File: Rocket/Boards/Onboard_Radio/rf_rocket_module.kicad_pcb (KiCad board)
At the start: 4 copper layers, 55 x 65 mm, 98 parts, among them J1 CAN1_T, J19 Backup Power, J2 CAN2_T, J3 DB9 Microfit, J4 USB_B_Micro, J5 SWD JST PH, J6 DB9 Microfit, Q1 DMP6023LFG, SW1 On Switch, U1 SX1262IMLTRT, U2 TCAN1046, U3 STM32G0B1RCTx, U4 AZ1117C-5.0, U5 TPS2121RUXR, U6 PE4259 RF Switch, U7 AZ1117C-3.3, Y1 8MHz

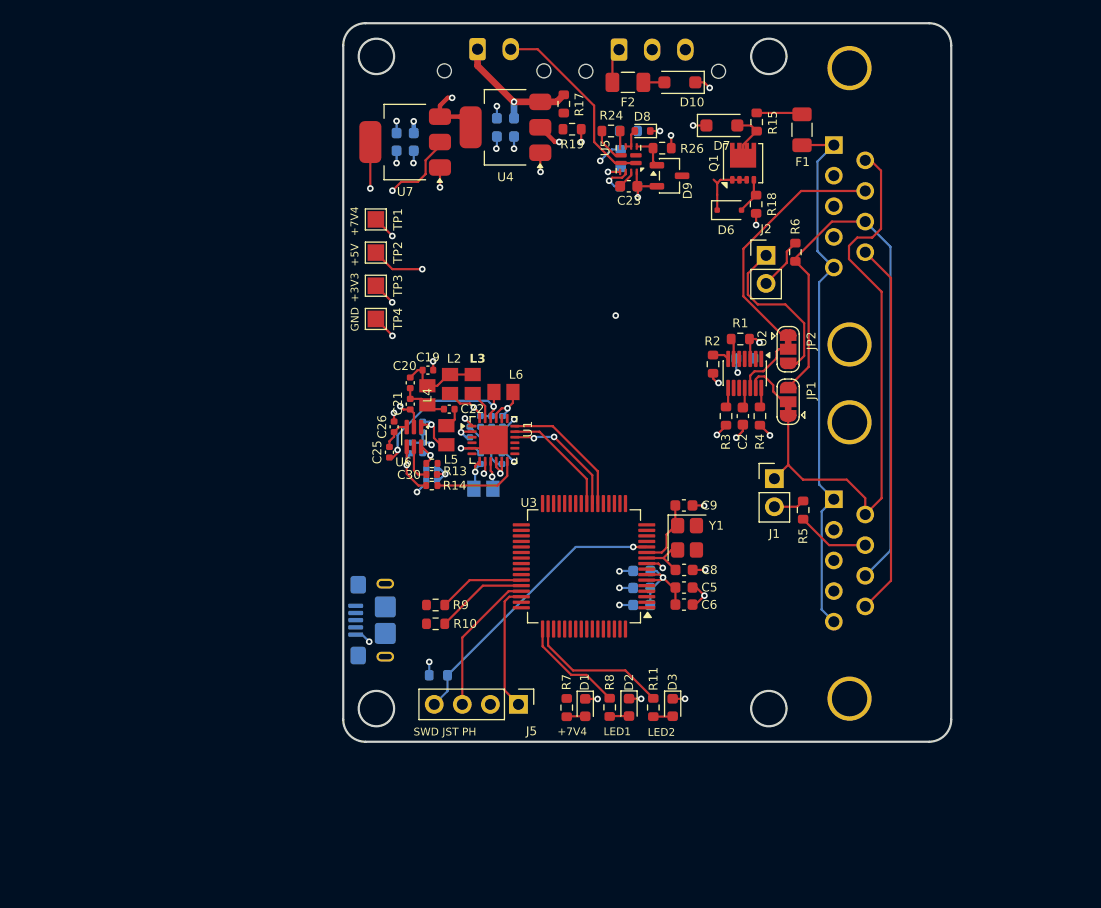
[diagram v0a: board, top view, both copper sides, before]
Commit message: schematic bom needs updating and traces need finishing
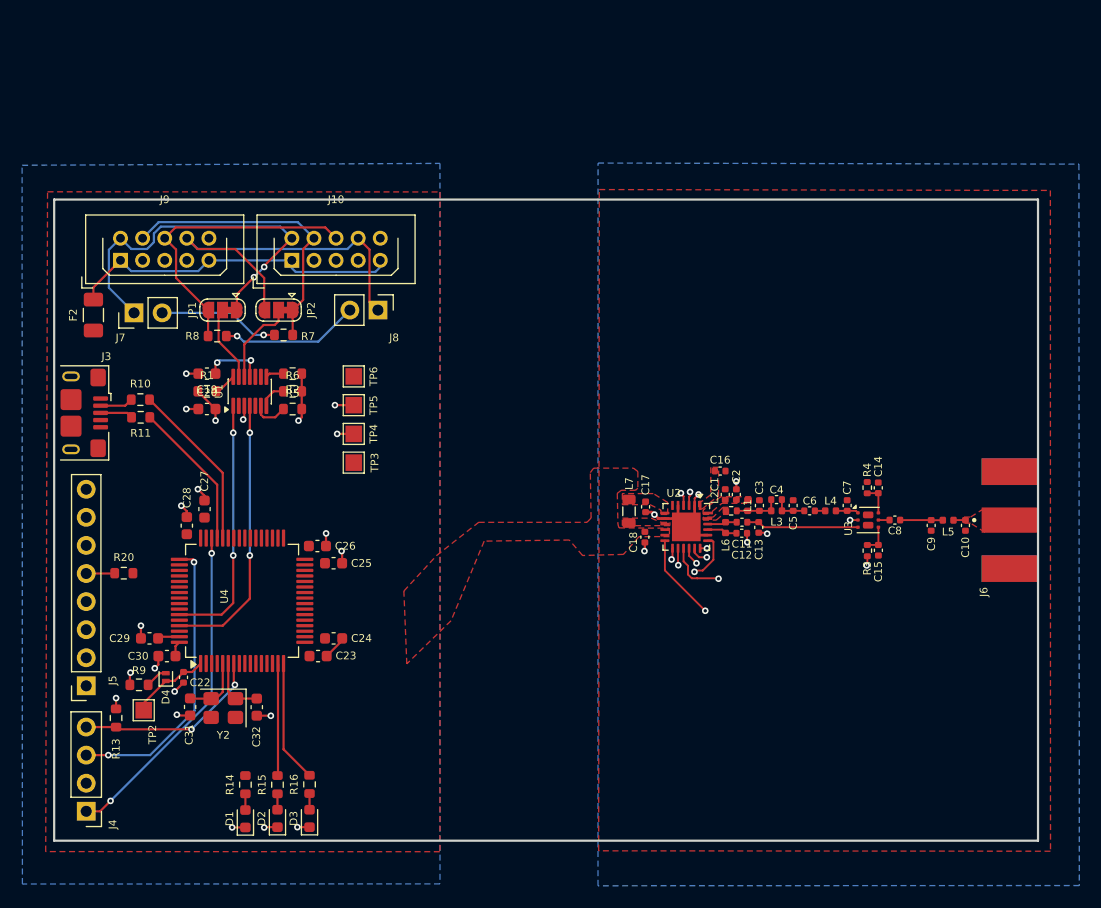
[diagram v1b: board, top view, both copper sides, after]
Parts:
- removed C21: C, Capacitor_SMD:C_0402_1005Metric
- removed D10, D7: 9V 15.4VC, Diode_SMD:D_SOD-123F
- removed D6: 18V, Diode_SMD:D_SOD-323F
- removed D8: D_0.5VF, Diode_SMD:D_SOD-523
- removed D9: 2.5V Ref Zener, Package_TO_SOT_SMD:SOT-23-3
- removed F1: 5A, Fuse:Fuse_1206_3216Metric
- removed H1, H2, H3, H4: MountingHole, MountingHole:MountingHole_3.2mm_M3
- removed J1: CAN1_T, Connector_PinHeader_2.54mm:PinHeader_1x02_P2.54mm_Vertical
- removed J19: Backup Power, Connector_Molex:Molex_Micro-Fit_3.0_43650-0315_1x03_P3.00mm_Vertical
- removed J2: CAN2_T, Connector_PinHeader_2.54mm:PinHeader_1x02_P2.54mm_Vertical
- removed Q1: DMP6023LFG, Package_SON:Diodes_PowerDI3333-8
- removed R12: R, Resistor_SMD:R_0603_1608Metric
- removed R17: 14K3, Resistor_SMD:R_0603_1608Metric
- removed R18: 100K, Resistor_SMD:R_0603_1608Metric
- removed R19: 9K53, Resistor_SMD:R_0603_1608Metric
- removed R22: 22K, Resistor_SMD:R_0603_1608Metric
- removed R23: 15K, Resistor_SMD:R_0603_1608Metric
- removed R24: 6K2, Resistor_SMD:R_0603_1608Metric
- removed R25: 4K7, Resistor_SMD:R_0603_1608Metric
- removed R26: 1K5, Resistor_SMD:R_0603_1608Metric
- removed SW1: On Switch, Connector_Molex:Molex_Micro-Fit_3.0_43650-0215_1x02_P3.00mm_Vertical
- removed TP1: 7V4, TestPoint:TestPoint_Pad_1.5x1.5mm
- removed U5: TPS2121RUXR, Package_DFN_QFN:Texas_VQFN-HR-12_2x2.5mm_P0.5mm
- removed U6: PE4259 RF Switch, Package_TO_SOT_SMD:SOT-363_SC-70-6
- removed U7: AZ1117C-3.3, Package_TO_SOT_SMD:SOT-223-3_TabPin2
- removed Y1: 8MHz, Crystal:Crystal_SMD_Abracon_ABM8G-4Pin_3.2x2.5mm
- added D4: D_Schottky, Diode_SMD:D_SOD-882, F.Cu at (115.6, 114.2)
- added J10: M80-5301042, Connector_Harwin:Harwin_LTek-Male_2x05_P2.00mm_Vertical, F.Cu at (127.0, 76.5)
- added J7: CAN1_T, Connector_PinHeader_2.54mm:PinHeader_1x02_P2.54mm_Vertical, F.Cu at (112.7, 81.2)
- added J8: CAN2_T, Connector_PinHeader_2.54mm:PinHeader_1x02_P2.54mm_Vertical, F.Cu at (134.8, 81.0)
- added J9: M80-5301042, Connector_Harwin:Harwin_LTek-Male_2x05_P2.00mm_Vertical, F.Cu at (111.5, 76.5)
- added L7: 15uH, Inductor_SMD:L_0805_2012Metric, F.Cu at (157.5, 99.2)
- added R16: 220R, Resistor_SMD:R_0603_1608Metric, F.Cu at (128.6, 123.9)
- added R20: 0R, Resistor_SMD:R_0603_1608Metric, F.Cu at (111.8, 104.8)
- added TP5: 3V3, TestPoint:TestPoint_Pad_1.5x1.5mm, F.Cu at (132.6, 89.6)
- added TP6: GND, TestPoint:TestPoint_Pad_1.5x1.5mm, F.Cu at (132.6, 87.0)
- added Y2: 12MHz, Crystal:Crystal_SMD_Abracon_ABM8G-4Pin_3.2x2.5mm, F.Cu at (120.8, 117.0)
- C1: value 100nF -> 47pF; footprint Capacitor_SMD:C_0603_1608Metric -> Capacitor_SMD:C_0402_1005Metric; moved to F.Cu
- C10: value C -> 3.3pF; moved to F.Cu
- C11: value 22uF -> 2.4pF; footprint Capacitor_SMD:C_0603_1608Metric -> Capacitor_SMD:C_0402_1005Metric; moved to F.Cu
- C12: value 10uF -> 1.8pF; footprint Capacitor_SMD:C_0603_1608Metric -> Capacitor_SMD:C_0402_1005Metric; moved to F.Cu
- C13: value 22uF -> ???; footprint Capacitor_SMD:C_0603_1608Metric -> Capacitor_SMD:C_0402_1005Metric; moved to F.Cu
- C14: value 10uF -> 1nF; footprint Capacitor_SMD:C_0603_1608Metric -> Capacitor_SMD:C_0402_1005Metric; moved to F.Cu
- C15: value 470nF -> 1nF; moved to F.Cu
- C16: value 100nF -> 1uF; moved to F.Cu
- C17: value C -> 470nF; moved to F.Cu
- C18: value C -> 100nF; moved to F.Cu
- C19, C20, C25: value C -> 100nF; footprint Capacitor_SMD:C_0402_1005Metric -> Capacitor_SMD:C_0603_1608Metric
- C2: value 100nF -> 47pF; footprint Capacitor_SMD:C_0603_1608Metric -> Capacitor_SMD:C_0402_1005Metric
- C22: value C -> 100n
- C24: value C -> 4.7uF; footprint Capacitor_SMD:C_0402_1005Metric -> Capacitor_SMD:C_0603_1608Metric; moved to F.Cu
- C26, C30: value C -> 4.7uF; footprint Capacitor_SMD:C_0402_1005Metric -> Capacitor_SMD:C_0603_1608Metric
- C27: value C -> 100nF; footprint Capacitor_SMD:C_0402_1005Metric -> Capacitor_SMD:C_0603_1608Metric; moved to F.Cu
- C28: value 1nF -> 4.7uF; footprint Capacitor_SMD:C_0402_1005Metric -> Capacitor_SMD:C_0603_1608Metric; moved to F.Cu
- C29: value 1nF -> 100nF; footprint Capacitor_SMD:C_0402_1005Metric -> Capacitor_SMD:C_0603_1608Metric; moved to F.Cu
- C3: value 100nF -> ???; footprint Capacitor_SMD:C_0603_1608Metric -> Capacitor_SMD:C_0402_1005Metric; moved to F.Cu
- C31, C32: value C -> 27pF; footprint Capacitor_SMD:C_0402_1005Metric -> Capacitor_SMD:C_0603_1608Metric; moved to F.Cu
- C4: value 100nF -> 3.0pF; footprint Capacitor_SMD:C_0603_1608Metric -> Capacitor_SMD:C_0402_1005Metric; moved to F.Cu
- C5: value 4.7uF -> 5.6pF; footprint Capacitor_SMD:C_0603_1608Metric -> Capacitor_SMD:C_0402_1005Metric
- C6: value 4.7uF -> 39pF; footprint Capacitor_SMD:C_0603_1608Metric -> Capacitor_SMD:C_0402_1005Metric
- C7: value 100nF -> 1.8pF; footprint Capacitor_SMD:C_0603_1608Metric -> Capacitor_SMD:C_0402_1005Metric; moved to F.Cu
- C8: value 27pF -> 39pF; footprint Capacitor_SMD:C_0603_1608Metric -> Capacitor_SMD:C_0402_1005Metric
- C9: value 27pF -> 3.3pF; footprint Capacitor_SMD:C_0603_1608Metric -> Capacitor_SMD:C_0402_1005Metric
- J3: value DB9 Microfit -> USB_B_Micro; footprint Connector_Dsub:DSUB-9_Pins_Horizontal_P2.77x2.84mm_EdgePinOffset7.70mm_Housed_MountingHolesOffset9.12mm -> Connector_USB:USB_Micro-B_Amphenol_10118193-0001LF_Horizontal; moved to F.Cu
- J4: value USB_B_Micro -> SWD JST PH; footprint Connector_USB:USB_Micro-B_Amphenol_10118193-0001LF_Horizontal -> Connector_PinHeader_2.54mm:PinHeader_1x04_P2.54mm_Vertical; moved to F.Cu
- J5: value SWD JST PH -> Conn_01x08; footprint Connector_PinHeader_2.54mm:PinHeader_1x04_P2.54mm_Vertical -> Connector_PinSocket_2.54mm:PinSocket_1x08_P2.54mm_Vertical
- J6: value DB9 Microfit -> RFIO SMA; footprint Connector_Dsub:DSUB-9_Pins_Horizontal_P2.77x2.84mm_EdgePinOffset7.70mm_Housed_MountingHolesOffset9.12mm -> Library:JOHNSON_142-0701-841; moved to F.Cu
- L1: value 15uH -> 47nH; footprint Library:INDC2012X145N -> Inductor_SMD:L_0402_1005Metric; moved to F.Cu
- L2: value L -> 0R; footprint Library:INDC2012X145N -> Resistor_SMD:R_0402_1005Metric
- L3: value L -> 2.5nH; footprint Library:INDC2012X145N -> Inductor_SMD:L_0402_1005Metric
- L4: value L -> 4.7nH; footprint Library:INDC2012X145N -> Inductor_SMD:L_0402_1005Metric
- L5: value L -> 9.1nH; footprint Library:INDC2012X145N -> Inductor_SMD:L_0402_1005Metric
- L6: value L -> 15nH; footprint Library:INDC2012X145N -> Inductor_SMD:L_0402_1005Metric
- R11: value 220R -> 27R
- R13: value 100R -> R; footprint Resistor_SMD:R_0402_1005Metric -> Resistor_SMD:R_0603_1608Metric
- R14: value 100R -> 549R; footprint Resistor_SMD:R_0402_1005Metric -> Resistor_SMD:R_0603_1608Metric
- R15: value 0R -> 220R
- R3, R4: value 100K -> 100R; footprint Resistor_SMD:R_0603_1608Metric -> Resistor_SMD:R_0402_1005Metric
- R5, R6: value 120R -> 100K
- R7: value 549R -> 120R
- R8: value 220R -> 120R
- R9: value 27R -> 33R
- TP2: value 5V -> RTC_CAP
- TP3: value 3V3 -> 7V4
- TP4: value GND -> 5V
- U1: value SX1262IMLTRT -> TCAN1046; footprint Package_DFN_QFN:QFN-24-1EP_4x4mm_P0.5mm_EP2.6x2.6mm -> Library:Texas_DYY0014A_TSOT-23-14
- U2: value TCAN1046 -> SX1262; footprint Library:Texas_DYY0014A_TSOT-23-14 -> Package_DFN_QFN:QFN-24-1EP_4x4mm_P0.5mm_EP2.6x2.6mm
- U3: value STM32G0B1RCTx -> PE4259 RF Switch; footprint Package_QFP:LQFP-64_10x10mm_P0.5mm -> Package_TO_SOT_SMD:Vishay_PowerPAK_SC70-6L_Dual
- U4: value AZ1117C-5.0 -> STM32H562RGT6; footprint Package_TO_SOT_SMD:SOT-223-3_TabPin2 -> Package_QFP:LQFP-64_10x10mm_P0.5mm
- moved R15 74.0 mm to (125.7, 123.9), turned to -90 degrees
- moved J3 73.1 mm to (107.0, 90.3)
- moved R11 53.3 mm to (113.3, 90.7), turned to 180 degrees
- moved F2 52.7 mm to (109.0, 81.5), turned to 90 degrees
- moved JP1 51.8 mm to (120.7, 81.0), turned to 180 degrees
- moved C23 50.9 mm to (129.4, 112.3), turned to 180 degrees
- moved U4 49.0 mm to (122.5, 107.3), turned to 90 degrees
- moved R8 48.9 mm to (120.2, 83.3), turned to 0 degrees
- moved R1 48.5 mm to (119.3, 88.4)
- moved C14 47.5 mm to (180.1, 97.1), turned to 90 degrees
- moved C12 47.3 mm to (167.7, 101.2), turned to 0 degrees
- moved R6 47.2 mm to (127.1, 88.4), turned to 0 degrees
- moved R5 47.1 mm to (127.1, 90.0), turned to 0 degrees
- moved TP2 46.4 mm to (113.6, 117.2), turned to 0 degrees
- moved JP2 46.2 mm to (125.8, 81.0), turned to 180 degrees
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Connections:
- C1 pad 1: +3V3 -> Net-(U2-VR_PA)
- C10 pad 1: VDD_Radio -> Net-(J6-In)
- C11 pad 1: +3V3 -> Net-(U2-RFI_N)
- C11 pad 2: GND -> Net-(U3-RF_2)
- C12 pad 1: +5V -> Net-(U2-RFI_P)
- C13 pad 1: +5V -> Net-(U3-RF_2)
- C14 pad 1: +7V4 -> Net-(U3-VDD)
- C15 pad 1: Net-(U1-VREG) -> Net-(U3-CTRL)
- C16 pad 1: VDD_Radio -> VDD_RADIO
- C17 pad 1: Net-(U1-VR_PA) -> Net-(U2-VREG)
- C18 pad 1: Net-(U1-VR_PA) -> VDD_RADIO
- C19 pad 1: Net-(C19-Pad1) -> +5V
- C2 pad 1: +5V -> Net-(U2-VR_PA)
- C20 pad 1: Net-(C19-Pad1) -> +3V3
- C20 pad 2: Net-(C20-Pad2) -> GND
- C22 pad 1: Net-(C20-Pad2) -> Net-(D4-K)
- C22 pad 2: Net-(C22-Pad2) -> GND
- C23 pad 1: Net-(U5-SS) -> +3V3
- C23 pad 2: Net-(D8-A) -> GND
- C24 pad 1: Net-(U6-RF_1) -> +3V3
- C25 pad 1: Net-(U1-RFI_N) -> +3V3
- C25 pad 2: Net-(U6-RF_2) -> GND
- C26 pad 1: GND -> +3V3
- C26 pad 2: Net-(U6-RF_2) -> GND
- C27 pad 1: GND -> +3V3
- C27 pad 2: Net-(U1-RFI_P) -> GND
- C28 pad 1: Net-(U6-VDD) -> +3V3
- C29 pad 1: Net-(U6-CTRL) -> +3V3
- C3 pad 1: +3V3 -> Net-(C3-Pad1)
- C30 pad 1: Net-(U6-RFC) -> +3V3
- C30 pad 2: Net-(J11-In) -> GND
- C31 pad 1: Net-(J11-In) -> GND
- C31 pad 2: GND -> Net-(U4-PH0)
- C32 pad 1: Net-(J11-In) -> Net-(U4-PH1)
- C4 pad 1: +3V3 -> Net-(C3-Pad1)
- C4 pad 2: GND -> Net-(C4-Pad2)
- C5 pad 1: +3V3 -> Net-(C4-Pad2)
- C6 pad 1: +3V3 -> Net-(C4-Pad2)
- C6 pad 2: GND -> Net-(C6-Pad2)
- C7 pad 1: +3V3 -> Net-(U3-RF_1)
- C8 pad 1: GND -> Net-(U3-RFC)
- C8 pad 2: Net-(U3-PF0) -> Net-(C8-Pad2)
- C9 pad 1: Net-(U3-PF1) -> Net-(C8-Pad2)
- F2 pad 1: Net-(D10-A2) -> +7V4
- J3 pad 1: Net-(F1-Pad2) -> unconnected-(J3-VBUS-Pad1)
- J3 pad 2: GND -> /MCU/USB_D-
- J3 pad 3: /CAN_Termination/CAN2_AUX -> /MCU/USB_D+
- J3 pad 4: GND -> unconnected-(J3-ID-Pad4)
- J3 pad 5: Net-(F1-Pad2) -> GND
- J4 pad 1: unconnected-(J4-VBUS-Pad1) -> /MCU/SWCLK
- J4 pad 2: /MCU/USB_D- -> GND
- J4 pad 3: /MCU/USB_D+ -> /MCU/SWDIO
- J4 pad 4: unconnected-(J4-ID-Pad4) -> /MCU/NRST
- J5 pad 1: /MCU/SWCLK -> GND
- J5 pad 2: GND -> unconnected-(J5-Pin_2-Pad2)
- J5 pad 3: /MCU/SWDIO -> unconnected-(J5-Pin_3-Pad3)
- J5 pad 4: /MCU/NRST -> unconnected-(J5-Pin_4-Pad4)
- J6 pad 1: Net-(F1-Pad2) -> Net-(J6-In)
- L1 pad 1: Net-(U1-DCC_SW) -> Net-(C3-Pad1)
- L1 pad 2: Net-(U1-VREG) -> Net-(U2-VR_PA)
- L2 pad 1: Net-(U1-VR_PA) -> Net-(U2-RFO)
- L2 pad 2: Net-(C19-Pad1) -> Net-(C3-Pad1)
- L3 pad 1: Net-(U1-RFO) -> Net-(C3-Pad1)
- L3 pad 2: Net-(C19-Pad1) -> Net-(C4-Pad2)
- L4 pad 1: Net-(C19-Pad1) -> Net-(C6-Pad2)
- L4 pad 2: Net-(C20-Pad2) -> Net-(U3-RF_1)
- L5 pad 1: Net-(C22-Pad2) -> Net-(C8-Pad2)
- L5 pad 2: Net-(U6-RF_1) -> Net-(J6-In)
- L6 pad 1: Net-(U1-RFI_P) -> Net-(U2-RFI_P)
- L6 pad 2: Net-(U1-RFI_N) -> Net-(U2-RFI_N)
- R1 pad 1: Net-(U2-TXD2) -> +3V3
- R1 pad 2: +3V3 -> Net-(U1-STB1)
- R10 pad 1: Net-(U3-PA10/PA12) -> /MCU/USB_D-
- R10 pad 2: /MCU/USB_D+ -> Net-(U4-PA11)
- R11 pad 1: /MCU/LED2 -> Net-(U4-PA12)
- R11 pad 2: Net-(D3-A) -> /MCU/USB_D+
- R13 pad 1: /LoRa Module/ANT_SW -> +3V3
- R13 pad 2: Net-(U6-VDD) -> /MCU/NRST
- R14 pad 1: /LoRa Module/DIO2 -> +7V4
- R14 pad 2: Net-(U6-CTRL) -> Net-(D1-A)
- R15 pad 1: /Power Input/PWR_OUT -> /MCU/LED1
- R15 pad 2: /CAN_Termination/CAN_PWR_IN -> Net-(D2-A)
- R2 pad 1: Net-(U2-RXD2) -> +3V3
- R2 pad 2: +3V3 -> Net-(U1-STB2)
- R3 pad 1: +3V3 -> /LoRav2/DIO2
- R3 pad 2: Net-(U2-STB2) -> Net-(U3-CTRL)
- R4 pad 1: +3V3 -> /LoRav2/ANT_SW
- R4 pad 2: Net-(U2-STB1) -> Net-(U3-VDD)
- R5 pad 1: Net-(J1-Pin_2) -> Net-(U1-TXD2)
- R5 pad 2: /CAN_Termination/CANL1 -> +3V3
- R6 pad 1: /CAN_Termination/CANH2 -> Net-(U1-RXD2)
- R6 pad 2: Net-(J2-Pin_2) -> +3V3
- R7 pad 1: +7V4 -> Net-(J7-Pin_2)
- R7 pad 2: Net-(D1-A) -> /CAN_Termination/CANL1
- R8 pad 1: /MCU/LED1 -> /CAN_Termination/CANH2
- R8 pad 2: Net-(D2-A) -> Net-(J8-Pin_2)
- R9 pad 1: /MCU/USB_D- -> Net-(D4-A)
- R9 pad 2: Net-(U3-PA9/PA11) -> +3V3
- TP2 pad 1: +5V -> Net-(D4-K)
- TP3 pad 1: +3V3 -> +7V4
- TP4 pad 1: GND -> +5V
- U1 pad 1: VDD_Radio -> /CAN_Termination/CAN1_TX
- U1 pad 10: VDD_Radio -> unconnected-(U1-CANH2-Pad10)
- U1 pad 11: VDD_Radio -> +5V
- U1 pad 12: /LoRa Module/DIO2 -> /CAN_Termination/CANL
- U1 pad 13: /LoRa Module/DIO1 -> /CAN_Termination/CANH
- U1 pad 14: /LoRa Module/BUSY -> Net-(U1-STB1)
- U1 pad 3: /LoRa Module/XTA -> +3V3
- U1 pad 4: /LoRa Module/XTB -> /CAN_Termination/CAN1_RX
- U1 pad 6: /LoRa Module/DIO3 -> Net-(U1-TXD2)
- U1 pad 7: Net-(U1-VREG) -> Net-(U1-RXD2)
- U1 pad 8: GND -> Net-(U1-STB2)
- U1 pad 9: Net-(U1-DCC_SW) -> unconnected-(U1-CANL2-Pad9)
- U2 pad 1: /CAN_Termination/CAN1_TX -> VDD_RADIO
- U2 pad 10: unconnected-(U2-CANH2-Pad10) -> VDD_RADIO
- U2 pad 11: +5V -> VDD_RADIO
- U2 pad 12: /CAN_Termination/CANL -> /LoRav2/DIO2
- U2 pad 13: /CAN_Termination/CANH -> /LoRav2/DIO1
- U2 pad 14: Net-(U2-STB1) -> /LoRav2/BUSY
- U2 pad 3: +3V3 -> /LoRav2/XTA
- U2 pad 4: /CAN_Termination/CAN1_RX -> /LoRav2/XTB
- U2 pad 6: Net-(U2-TXD2) -> /LoRav2/DIO3
- U2 pad 7: Net-(U2-RXD2) -> Net-(U2-VREG)
- U2 pad 8: Net-(U2-STB2) -> GND
- U2 pad 9: unconnected-(U2-CANL2-Pad9) -> Net-(U2-DCC_SW)
- U3 pad 1: /MCU/PWR_SOURCE -> Net-(U3-RF_1)
- U3 pad 2: unconnected-(U3-PC12-Pad2) -> GND
- U3 pad 3: unconnected-(U3-PC13-Pad3) -> Net-(U3-RF_2)
- U3 pad 4: unconnected-(U3-PC14-Pad4) -> Net-(U3-CTRL)
- U3 pad 5: unconnected-(U3-PC15-Pad5) -> Net-(U3-RFC)
- U3 pad 6: +3V3 -> Net-(U3-VDD)
- U4 pad 1: GND -> Net-(D4-K)
- U4 pad 2: +5V -> unconnected-(U4-PC13-Pad2)
- U4 pad 3: +7V4 -> unconnected-(U4-PC14-Pad3)
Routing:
- net Net-(F1-Pad2): track 49.3 -> 0.00 mm
- net /LoRav2/SCK: track 0.00 -> 39.8 mm, vias 0 -> 1
- net /LoRav2/MOSI: track 0.00 -> 38.4 mm, vias 0 -> 1
- net /LoRav2/NSS: track 0.00 -> 37.9 mm, vias 0 -> 1
- net /LoRav2/MISO: track 0.00 -> 35.3 mm, vias 0 -> 1
- net +7V4: track 32.6 -> 0.00 mm, vias 2 -> 0
- net /LoRav2/BUSY: track 0.00 -> 31.1 mm, vias 0 -> 1
- net /LoRav2/DIO1: track 0.00 -> 29.6 mm, vias 0 -> 1
- net GND: track 55.6 -> 27.6 mm, vias 34 -> 15
- net /CAN_Termination/CANH2: track 54.6 -> 26.8 mm
- net Net-(J10-Pin_1): track 3.21 -> 30.5 mm
- net /LoRav2/DIO2: track 0.00 -> 25.0 mm, vias 0 -> 2
- net /CAN_Termination/CAN1_RX: track 0.00 -> 24.8 mm, vias 0 -> 2
- net /CAN_Termination/CAN1_TX: track 0.00 -> 23.1 mm, vias 0 -> 2
- net Net-(D8-A): track 20.0 -> 0.00 mm, vias 2 -> 0
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- added copper zone on In2.Cu, net (none)
- added copper zone on B.Cu, net GND
- added copper zone on F.Cu, net GND
- added copper zone on F.Cu, net Net-(J6-In)
- added copper zone on F.Cu, net Net-(U2-DCC_SW)
- added copper zone on F.Cu, net Net-(U2-RFO)
- added copper zone on F.Cu, net Net-(U2-VREG)
- added copper zone on F.Cu, net Net-(U2-VR_PA)
- added copper zone on F.Cu, net VDD_RADIO
- removed copper zone on In2.Cu, net +5V
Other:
- board size 55 x 65 mm -> 89 x 58 mm
- board text removed: "+3V3"
- board text removed: "+5V"
- board text removed: "+7V4"
- board text removed: "GND"
- board text removed: "LED1"
- board text removed: "LED2"
- board text removed: "SWD JST PH"

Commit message: pcb done, need schematic review
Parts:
- added C33: 2u2, Resistor_SMD:R_0603_1608Metric, F.Cu at (131.7, 103.9)
- added C34: 2u2, Resistor_SMD:R_0603_1608Metric, F.Cu at (114.1, 109.2)
- added R12: 10k, Resistor_SMD:R_0603_1608Metric, F.Cu at (114.1, 107.6)
- added R17: 0R, Resistor_SMD:R_0603_1608Metric, F.Cu at (111.8, 97.2)
- added R18: 0R, Resistor_SMD:R_0603_1608Metric, F.Cu at (111.8, 99.7)
- added R19: 0R, Resistor_SMD:R_0603_1608Metric, F.Cu at (111.8, 102.3)
- added R21: 0R, Resistor_SMD:R_0603_1608Metric, F.Cu at (131.0, 107.1)
- TP2, TP3, TP4, TP5, TP6: footprint TestPoint:TestPoint_Pad_1.5x1.5mm -> TestPoint:TestPoint_Pad_1.0x1.0mm
- moved TP3 5.46 mm to (138.0, 94.0)
- moved TP4 5.45 mm to (138.0, 91.5), turned to 90 degrees
- moved TP5 5.43 mm to (138.0, 89.0)
- moved TP6 5.42 mm to (138.0, 86.5)
- moved C25 2.40 mm to (130.1, 101.6), turned to -90 degrees
- moved C26 1.10 mm to (128.5, 101.6), turned to -90 degrees
- moved J6 0.54 mm to (193.9, 100.0)
- moved C10 0.34 mm to (187.6, 100.5)
- moved C9 0.34 mm to (184.5, 100.5)
- moved L5 0.34 mm to (186.0, 100.0)
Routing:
- net +7V4: track 0.00 -> 77.2 mm, vias 0 -> 4
- net /LoRav2/ANT_SW: track 0.00 -> 59.0 mm, vias 0 -> 2
- net GND: track 27.6 -> 68.7 mm, vias 15 -> 28
- net VDD_RADIO: track 0.00 -> 39.3 mm, vias 0 -> 4
- net /LoRav2/NSS: track 37.9 -> 3.58 mm
- net +5V: track 17.8 -> 44.0 mm, vias 3 -> 4
- net /LoRav2/SX_NRESET: track 19.8 -> 33.4 mm, vias 1 -> 2
- net /LoRav2/DIO1: track 29.6 -> 35.0 mm, vias 1 -> 2
- net /LoRav2/BUSY: track 31.1 -> 36.0 mm, vias 1 -> 2
- net /LoRav2/MISO: track 35.3 -> 39.2 mm, vias 1 -> 2
- net Net-(C33-Pad1): track 0.00 -> 2.97 mm
- net Net-(U4-BOOT0): track 0.00 -> 2.67 mm
- net /Power Input/+3V3: track 0.00 -> 2.63 mm
- net /Power Input/+3V3A: track 0.00 -> 2.62 mm
- net /Power Input/+5V: track 0.00 -> 2.60 mm
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- added copper zone on In2.Cu, net GND
- removed copper zone on In2.Cu, net (none)

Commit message: pcb updates
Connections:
- U1 pad 6: Net-(U1-TXD2) -> /CAN_Termination/CAN2_TX
- U1 pad 7: Net-(U1-RXD2) -> /CAN_Termination/CAN2_RX
- U4 pad 20: /MCU/SX1262_CS -> /LoRav2/NSS
- U4 pad 59: /CAN_Termination/CAN1_TX -> /CAN_Termination/CAN1_RX
- U4 pad 61: /CAN_Termination/CAN1_RX -> /CAN_Termination/CAN1_TX

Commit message: jpole project created
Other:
- board text added: "MANUFACTURE WITH ENIG"
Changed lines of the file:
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@@
 		(layer "Edge.Cuts")
+	)
+	(gr_text "MANUFACTURE WITH ENIG"
+		(at 15.5 18 0)
+		(layer "F.Cu")
+		(effects
+			(font
+				(size 1.5 1.5)
+				(thickness 0.3)
+				(bold yes)
+			)
+			(justify left bottom)
+		)
 	)
 	(segment

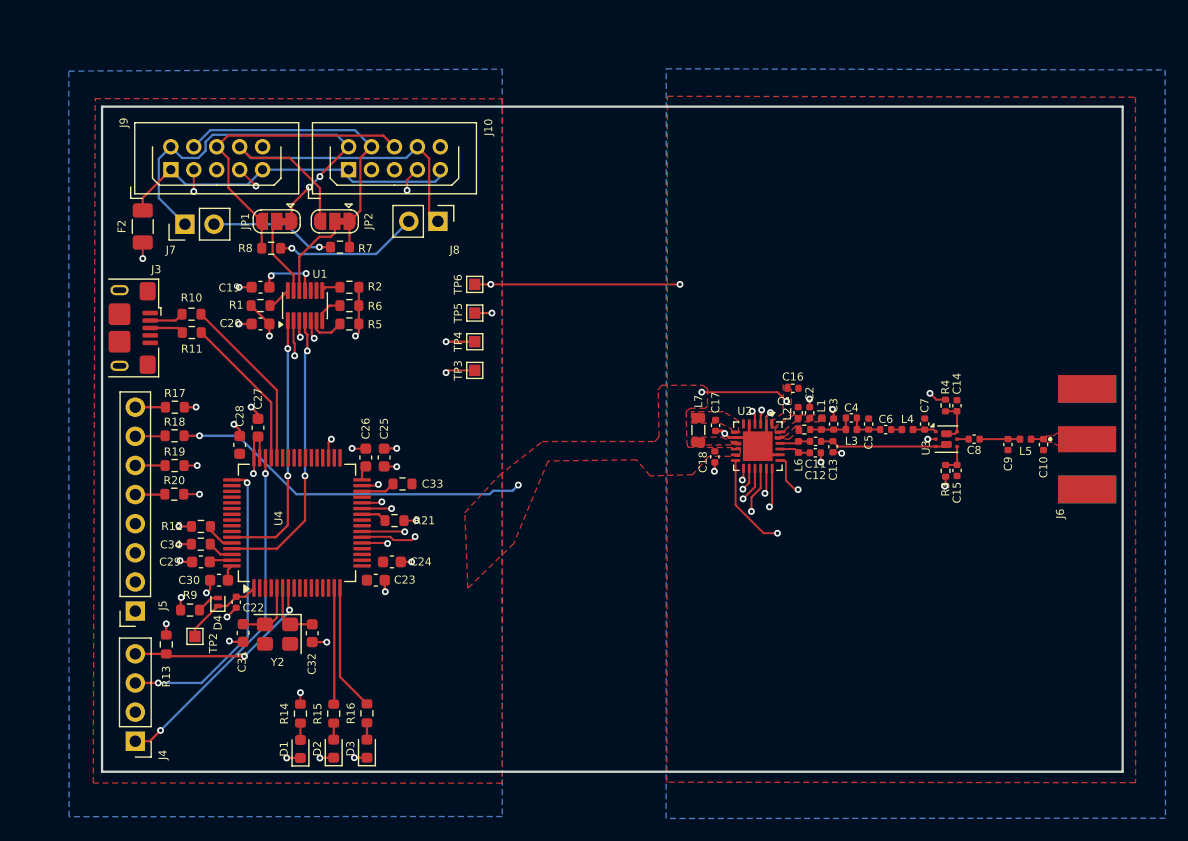
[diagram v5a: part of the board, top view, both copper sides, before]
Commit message: radio ic board planes joined, pcb made smaller, need to add cantraces before review
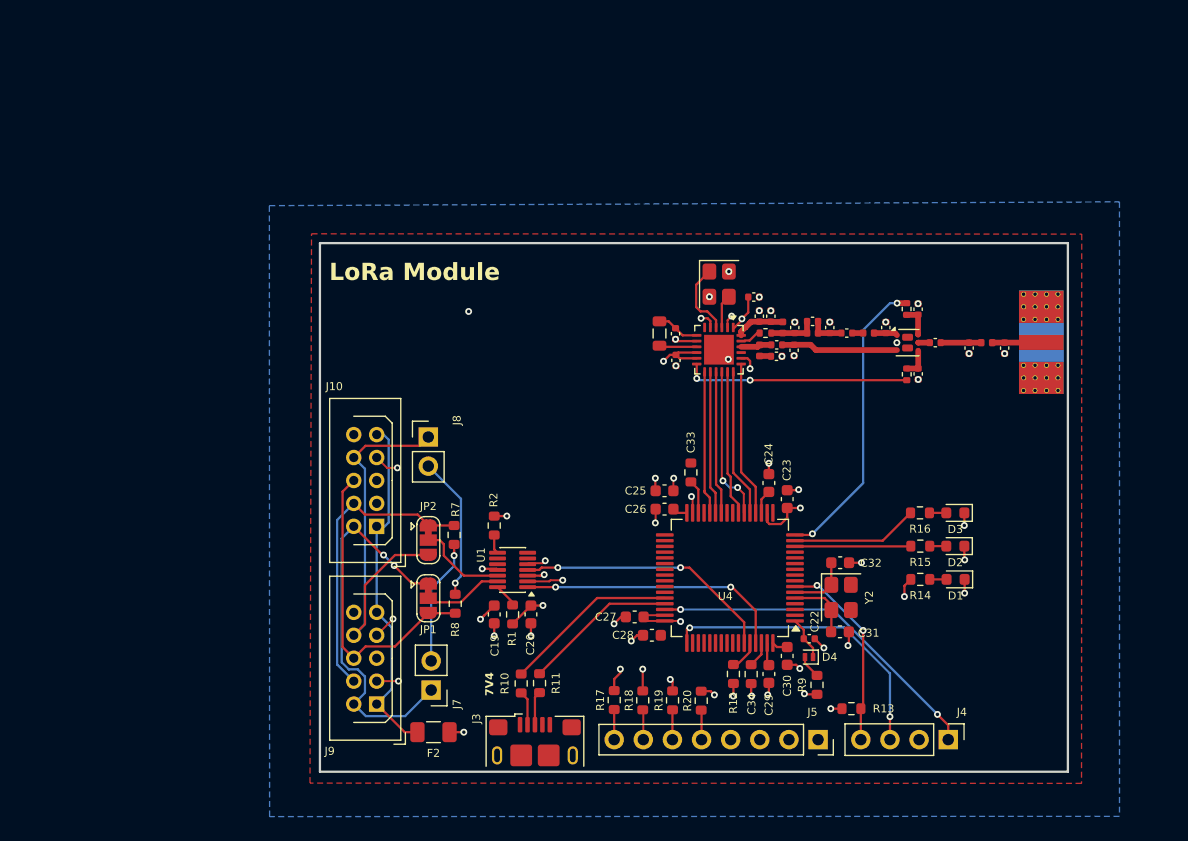
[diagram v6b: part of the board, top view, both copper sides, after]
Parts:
- removed R21: 0R, Resistor_SMD:R_0603_1608Metric
- removed R5, R6: 100K, Resistor_SMD:R_0603_1608Metric
- removed TP2: RTC_CAP, TestPoint:TestPoint_Pad_1.0x1.0mm
- removed TP3: 7V4, TestPoint:TestPoint_Pad_1.0x1.0mm
- removed TP4: 5V, TestPoint:TestPoint_Pad_1.0x1.0mm
- removed TP5: 3V3, TestPoint:TestPoint_Pad_1.0x1.0mm
- removed TP6: GND, TestPoint:TestPoint_Pad_1.0x1.0mm
- added Y1: 32.000MHz, Crystal:Crystal_SMD_Abracon_ABM8G-4Pin_3.2x2.5mm, F.Cu at (159.3, 86.5)
- J6: footprint Library:JOHNSON_142-0701-841 -> Library:SMA-KE-16.5A_EdgeMount
- moved J4 70.9 mm to (179.3, 126.2), turned to -90 degrees
- moved J5 60.6 mm to (167.9, 126.2), turned to -90 degrees
- moved R13 60.0 mm to (170.8, 123.5), turned to 0 degrees
- moved D1 59.0 mm to (179.9, 112.2), turned to 180 degrees
- moved D2 57.0 mm to (179.9, 109.3), turned to 180 degrees
- moved R14 55.3 mm to (176.9, 112.2), turned to 0 degrees
- moved D3 55.3 mm to (179.9, 106.4), turned to 180 degrees
- moved R9 55.1 mm to (167.8, 121.4), turned to -90 degrees
- moved R15 53.2 mm to (176.9, 109.3), turned to 0 degrees
- moved C31 52.1 mm to (169.8, 116.8), turned to 180 degrees
- moved J3 52.0 mm to (143.2, 127.6), turned to 0 degrees
- moved D4 51.8 mm to (167.2, 119.0), turned to 180 degrees
- moved R16 51.3 mm to (176.8, 106.4), turned to 0 degrees
- moved F2 50.9 mm to (134.4, 125.5), turned to 180 degrees
- moved C29 50.5 mm to (163.7, 120.5), turned to 90 degrees
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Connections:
- U4 pad 14: unconnected-(U4-PA0-Pad14) -> /MCU/LED1
- U4 pad 15: /MCU/LED1 -> /MCU/LED2
- U4 pad 16: /MCU/LED2 -> /LoRav2/ANT_SW
- U4 pad 26: /MCU/SX1262_RESET -> /LoRav2/SX_NRESET
- U4 pad 35: /LoRav2/ANT_SW -> unconnected-(U4-PB14-Pad35)
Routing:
- net /LoRav2/ANT_SW: track 59.0 -> 25.9 mm
- net /LoRav2/SCK: track 40.3 -> 12.9 mm, vias 2 -> 0
- net /LoRav2/MOSI: track 38.8 -> 12.7 mm, vias 2 -> 0
- net /LoRav2/MISO: track 39.2 -> 13.5 mm
- net +7V4: track 77.2 -> 52.7 mm, vias 4 -> 3
- net /LoRav2/BUSY: track 36.0 -> 12.5 mm, vias 2 -> 0
- net /LoRav2/DIO1: track 35.0 -> 12.5 mm, vias 2 -> 0
- net /LoRav2/SX_NRESET: track 33.4 -> 12.5 mm, vias 2 -> 0
- net GND: track 68.7 -> 48.1 mm, vias 28 -> 41
- net +5V: track 44.0 -> 28.1 mm, vias 4 -> 3
- net /LoRav2/NSS: track 3.58 -> 13.5 mm, vias 1 -> 0
- net VDD_RADIO: track 39.3 -> 47.1 mm, vias 4 -> 3
- net /LoRav2/DIO2: track 25.7 -> 19.6 mm
- net /LoRav2/XTB: track 1.21 -> 6.42 mm, vias 1 -> 0
- net Net-(U2-VR_PA): track 0.00 -> 4.33 mm
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- removed copper zone on In2.Cu, net GND
- removed copper zone on F.Cu, net Net-(J6-In)
- removed copper zone on F.Cu, net Net-(U2-DCC_SW)
- removed copper zone on F.Cu, net Net-(U2-RFO)
- removed copper zone on F.Cu, net Net-(U2-VREG)
- removed copper zone on F.Cu, net Net-(U2-VR_PA)
- removed copper zone on F.Cu, net VDD_RADIO
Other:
- board size 89 x 58 mm -> 65.2 x 46.1 mm
- board text added: "7V4"
- board text added: "J. Tomkins"
- board text added: "LoRa Module"

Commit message: schematic ready for review
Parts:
- removed R13: R, Resistor_SMD:R_0603_1608Metric
- moved C20 5.18 mm to (146.9, 112.0), turned to 0 degrees
- moved R1 1.07 mm to (142.1, 114.5), turned to 180 degrees
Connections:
- R1 pad 1: +3V3 -> /CAN_Termination/CAN_STB1
- U1 pad 6: /CAN_Termination/CAN2_TX -> unconnected-(U1-TXD2-Pad6)
- U1 pad 7: /CAN_Termination/CAN2_RX -> unconnected-(U1-RXD2-Pad7)
- U1 pad 8: Net-(U1-STB2) -> unconnected-(U1-STB2-Pad8)
- U4 pad 41: unconnected-(U4-PA8-Pad41) -> /CAN_Termination/CAN1_AUX
- U4 pad 42: unconnected-(U4-PA9-Pad42) -> /CAN_Termination/CAN_STB1
- U4 pad 43: unconnected-(U4-PA10-Pad43) -> /CAN_Termination/CAN2_AUX
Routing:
- net /CAN_Termination/CAN1_AUX: track 0.00 -> 28.7 mm
- net /CAN_Termination/CAN2_AUX: track 0.00 -> 27.5 mm
- net /CAN_Termination/CAN_STB1: track 0.00 -> 12.4 mm
- net GND: track 48.1 -> 47.1 mm
- net +3V3: track 19.4 -> 18.9 mm, vias 14 -> 12
